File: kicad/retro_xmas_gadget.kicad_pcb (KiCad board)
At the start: 4 copper layers, 76.2 x 101.6 mm, 84 parts, among them J1 USB_C_Receptacle_USB2.0_16P, J2 SD_Card_Receptacle, J3 AudioJack3_SwitchTR, J4 Conn_01x18, J5 Conn_01x02, J6 Conn_01x03, J7 Conn_01x03, J8 Conn_01x07, Q1 UMH3N, Q2 SS8050, SW1 RESET, SW10 SELECT, SW11 START, SW12 A, SW13 B, SW2 BOOT, SW3 KH-SS12F23-G6, SW4 UP, SW5 DOWN, SW6 LEFT, SW7 RIGHT, SW8 MENU, SW9 OPTION, U1 CP2102N-Axx-xQFN28, U2 ESP32-S3-WROOM-1, U4 XC6210B332MR, U5 TP4056

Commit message: improvements and corrections
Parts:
- D1: footprint Diode_SMD:D_SOD-323_HandSoldering -> Diode_SMD:D_SOD-123
- R23: value 5.1k -> 0R
- U3, U5: footprint Package_SO:SOP-8-1EP_4.57x4.57mm_P1.27mm_EP4.57x4.45mm_ThermalVias -> Package_SO:SOIC-8-1EP_3.9x4.9mm_P1.27mm_EP2.41x3.3mm_ThermalVias
- moved C15 9.08 mm to (77.7, 69.3), turned to 0 degrees
- moved C16 4.81 mm to (86.9, 68.5), turned to 0 degrees
- moved J5 3.52 mm to (79.4, 75.3)
- moved C10 3.43 mm to (87.0, 72.3)
- moved C9 3.43 mm to (87.0, 70.5)
- moved U3 1.84 mm to (87.0, 77.5)
- moved R15 1.02 mm to (41.9, 69.3)
- moved R16 1.02 mm to (41.9, 72.9)
- moved L1 0.51 mm to (77.7, 67.2)
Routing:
- net GND: track 100.0 -> 106.6 mm, vias 190 -> 185
- net VCC: track 29.2 -> 33.5 mm
- net /AUDIO+: track 10.8 -> 14.4 mm
- net VBUS: track 81.7 -> 85.1 mm
- net /SPK+: track 11.8 -> 14.4 mm
- net VAA: track 9.72 -> 11.9 mm
- net Net-(U5-PROG): track 2.90 -> 4.57 mm
- net /VBAT: track 34.1 -> 35.6 mm
- net Net-(D3-K): track 89.5 -> 90.6 mm
- net Net-(D4-K): track 85.1 -> 85.9 mm
- net Net-(U5-~{CHRG}): track 2.81 -> 3.47 mm
- net Net-(U5-~{STDBY}): track 2.80 -> 3.46 mm

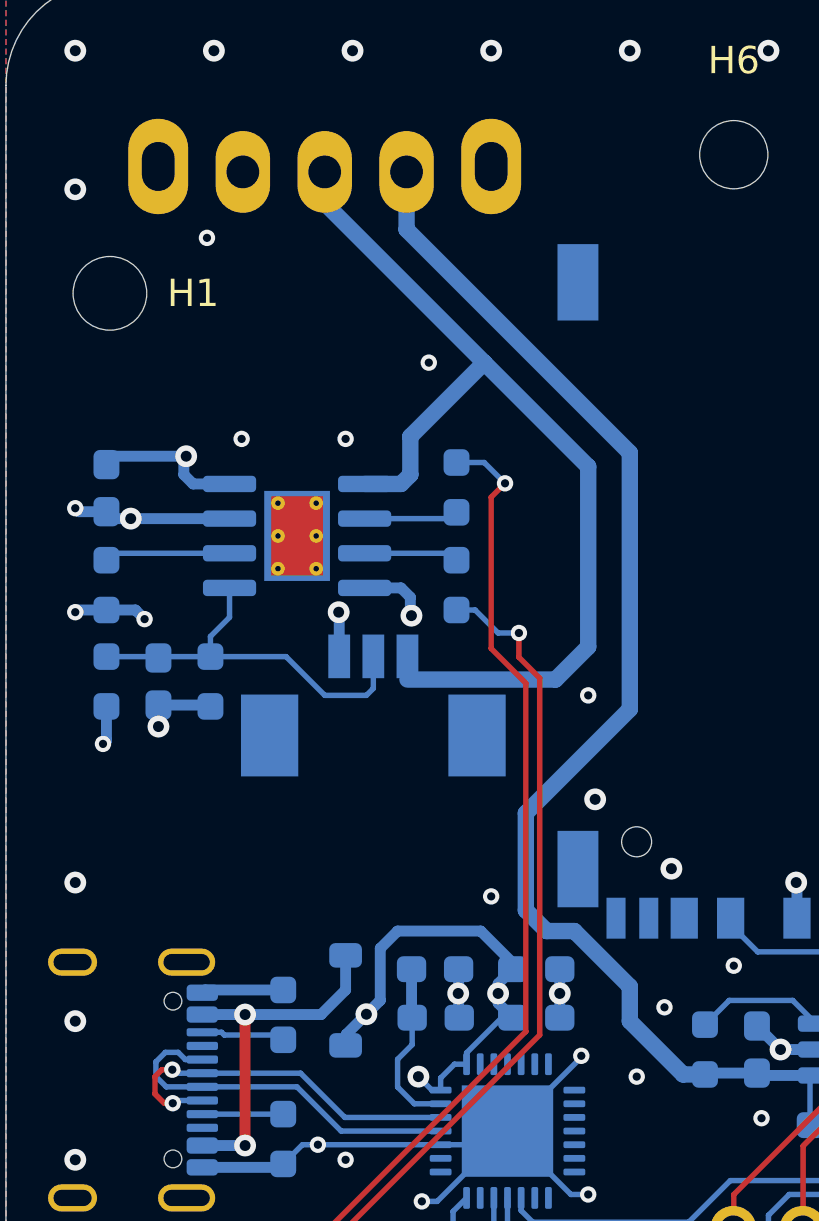
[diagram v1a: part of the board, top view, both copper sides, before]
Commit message: load sharing
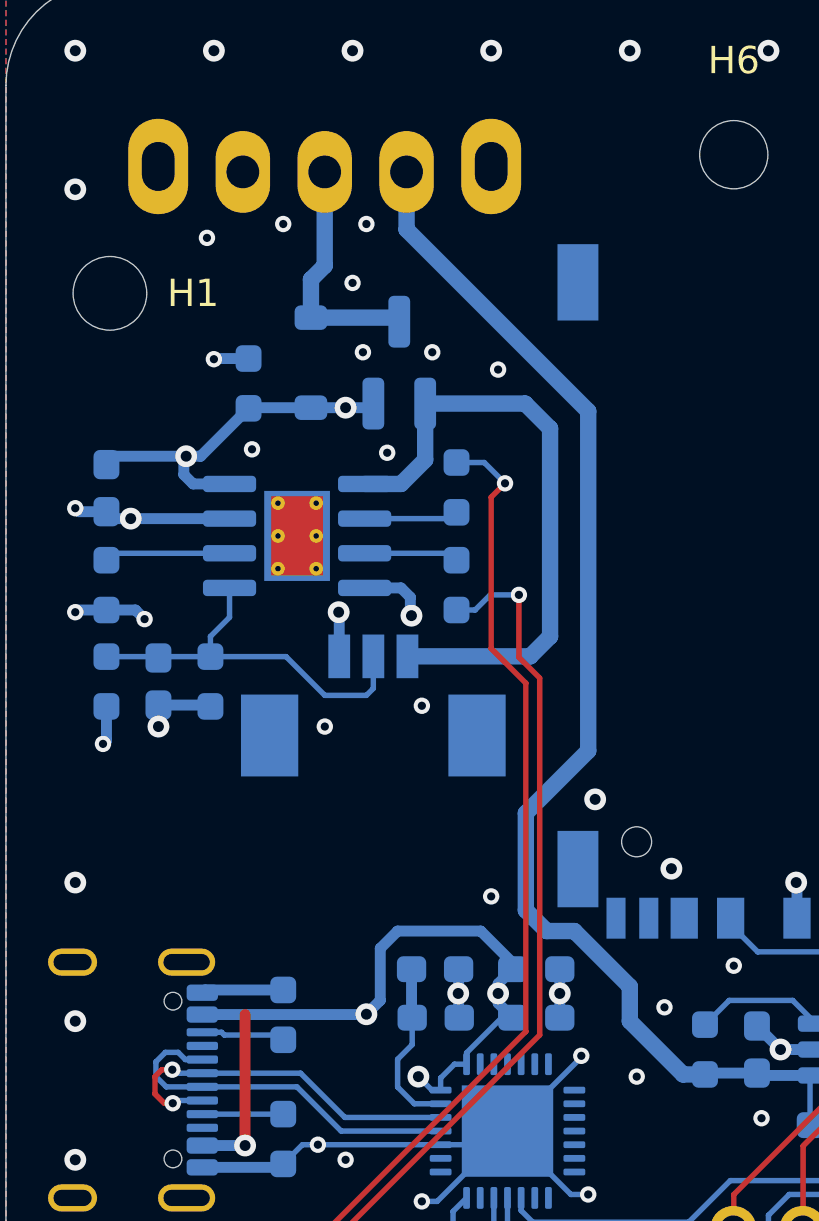
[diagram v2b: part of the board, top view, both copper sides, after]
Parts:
- added Q3: PMOS, Package_TO_SOT_SMD:SOT-23_Handsoldering, B.Cu at (39.8, 64.8)
- added R24: 100K, Resistor_SMD:R_0603_1608Metric_Pad0.98x0.95mm_HandSolder, B.Cu at (34.3, 65.5)
- D1: value BAT54J -> CRS08
- R14: value 2K -> 1.5K
- moved G*** 36.3 mm to (36.4, 100.1)
- moved D1 23.4 mm to (36.6, 64.8), turned to -90 degrees
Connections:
- D1 pad 1: VBUS -> /VBAT_LOAD
- D1 pad 2: Net-(D1-A) -> VBUS
- J1 pad A4: Net-(D1-A) -> VBUS
- J1 pad A9: Net-(D1-A) -> VBUS
- J1 pad B4: Net-(D1-A) -> VBUS
- J1 pad B9: Net-(D1-A) -> VBUS
- SW3 pad 2: /VBAT -> /VBAT_LOAD
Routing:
- net VBUS: track 85.1 -> 103.7 mm, vias 9 -> 11
- net Net-(D1-A): track 13.3 -> 0.00 mm, vias 2 -> 0
- net /VBAT: track 35.6 -> 22.8 mm
- net /VBAT_LOAD: track 0.00 -> 8.85 mm
- net GND: track 106.6 -> 107.8 mm, vias 185 -> 192
- net Net-(D4-K): track 85.9 -> 87.2 mm
- net /VBAT_ON: track 48.4 -> 47.1 mm

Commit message: rearrangement, updates, upgrades
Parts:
- moved G*** 71.7 mm to (96.8, 61.3)
- moved G*** 71.7 mm to (37.6, 99.3)
- moved H1 7.62 mm to (29.2, 54.6)
- moved H2 7.62 mm to (97.8, 54.6)
- moved SW3 2.80 mm to (36.9, 57.8)
- moved J2 2.22 mm to (62.2, 73.2)
- moved U3 2.09 mm to (89.1, 77.5)
- moved J5 1.91 mm to (81.3, 75.3)
- moved J3 1.82 mm to (90.2, 56.7)
- moved C16 1.78 mm to (88.6, 68.5)
- moved R10 1.78 mm to (93.2, 68.0)
- moved R9 1.78 mm to (93.2, 71.5)
- moved C10 1.78 mm to (88.8, 72.3)
- moved C15 1.78 mm to (79.5, 69.3)
- moved C9 1.78 mm to (88.8, 70.5)
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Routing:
- net /SD_DAT: track 35.7 -> 29.8 mm
- net GND: track 107.8 -> 103.5 mm, vias 192 -> 189
- net /VBAT_ON: track 47.1 -> 43.6 mm
- net VCC: track 33.5 -> 36.4 mm
- net VBUS: track 103.7 -> 106.2 mm
- net /TFT_LEDK: track 14.0 -> 16.4 mm
- net /AMP_LRCLK: track 2.83 -> 4.95 mm
- net /SD_CD: track 16.4 -> 14.3 mm
- net /SD_CLK: track 27.1 -> 25.1 mm
- net /SD_CMD: track 20.6 -> 19.0 mm
- net /HJ+: track 27.2 -> 25.8 mm
- net /TFT_LEDA: track 13.6 -> 14.9 mm
- net /RXD: track 59.3 -> 58.0 mm
- net /RTS: track 29.5 -> 28.2 mm
- net Net-(U1-D+): track 13.8 -> 15.0 mm
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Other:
- board text added: "CROKPOCKET XL"
- board text added: "https://github.com/ducalex/retro-go PCB v1.0 by hfvermeer"
- board text removed: "https://github.com/ducalex/retro-go PCB v0.9 by hfvermeer"

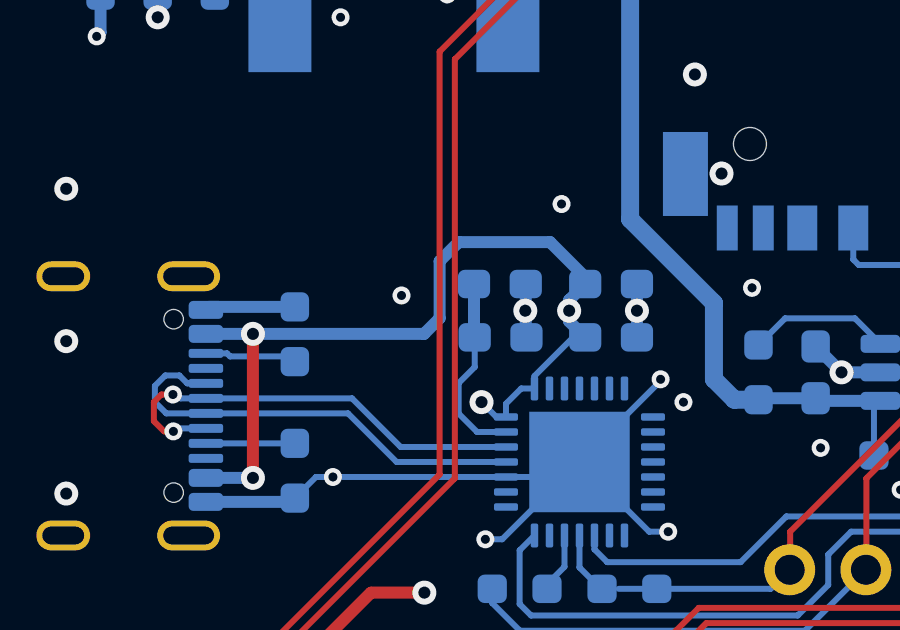
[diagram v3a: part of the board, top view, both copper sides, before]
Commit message: add pull up resistor to cp2102 rst
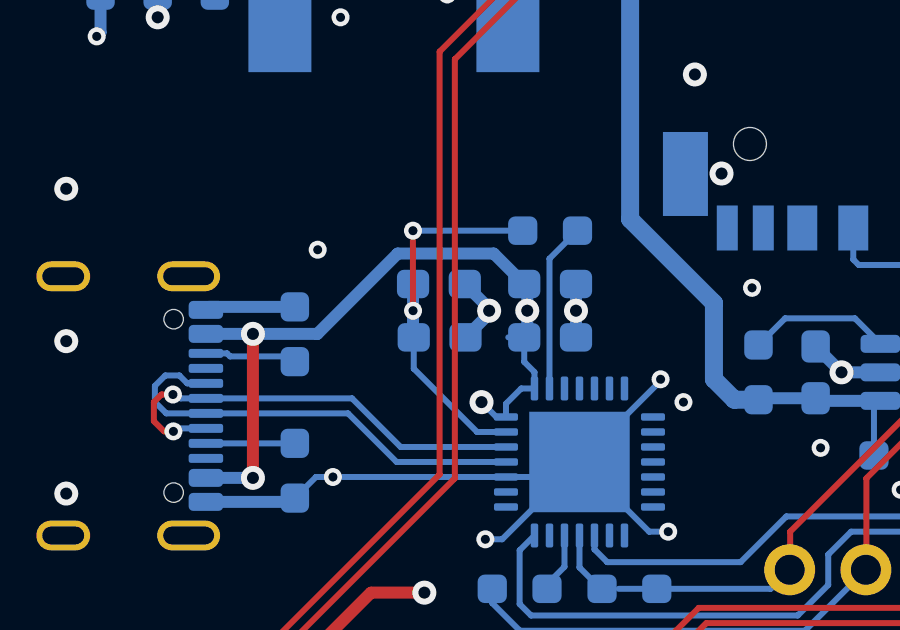
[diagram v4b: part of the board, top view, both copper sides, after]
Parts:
- added R25: 4.7k, Resistor_SMD:R_0603_1608Metric_Pad0.98x0.95mm_HandSolder, B.Cu at (44.1, 85.2)
- moved C4 2.03 mm to (40.4, 87.0)
- moved C1 2.03 mm to (44.1, 88.8)
- moved C2 2.03 mm to (44.1, 87.0)
- moved C3 2.03 mm to (40.4, 88.8)
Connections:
- U1 pad 9: unconnected-(U1-~{RST}-Pad9) -> Net-(U1-~{RST})
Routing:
- net Net-(U1-VDD): track 6.38 -> 13.1 mm, vias 0 -> 2
- net Net-(U1-~{RST}): track 0.00 -> 5.65 mm
- net VBUS: track 106.2 -> 102.2 mm
- net GND: track 103.5 -> 104.2 mm, vias 189 -> 188

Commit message: design check. Gerbers
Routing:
- net /TXD: track 52.3 -> 51.0 mm
- net VBUS: track 102.2 -> 101.7 mm
- net GND: track 104.2 -> 104.3 mm, vias 188 -> 195
- net (no net): vias 1 -> 0
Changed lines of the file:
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@@
 		)
 	)
-	(via
-		(at 50.8 160.02)
-		(size 0.8)
-		(drill 0.4)
-		(layers "F.Cu" "B.Cu")
-		(net 0)
-	)
 	(segment
 		(start 91.42 102.772134)
@@
 	)
 	(via
+		(at 45.466 83.82)
+		(size 0.6)
+		(drill 0.3)
+		(layers "F.Cu" "B.Cu")
+		(free yes)
+		(net 4)
+	)
+	(via
 		(at 27.94 70.104)
 		(size 0.6)
@@
 	)
 	(via
+		(at 45.466 76.454)
+		(size 0.6)
+		(drill 0.3)
+		(layers "F.Cu" "B.Cu")
+		(free yes)
+		(net 4)
+	)
+	(via
 		(at 79.248 106.426)
 		(size 0.6)
@@
 	)
 	(via
+		(at 41.91 84.074)
+		(size 0.6)
+		(drill 0.3)
+		(layers "F.Cu" "B.Cu")
+		(free yes)
+		(net 4)
+	)
+	(via
 		(at 83.058 96.52)
 		(size 0.6)
@@
 	)
 	(via
+		(at 94.742 69.088)
+		(size 0.6)
+		(drill 0.3)
+		(layers "F.Cu" "B.Cu")
+		(free yes)
+		(net 4)
+	)
+	(via
 		(at 42.672 102.616)
 		(size 0.6)
@@
 	)
 	(via
+		(at 44.45 59.69)
+		(size 0.6)
+		(drill 0.3)
+		(layers "F.Cu" "B.Cu")
+		(free yes)
+		(net 4)
+	)
+	(via
 		(at 78.867 113.538)
 		(size 0.6)
@@
 	)
 	(via
+		(at 42.164 81.026)
+		(size 0.6)
+		(drill 0.3)
+		(layers "F.Cu" "B.Cu")
+		(free yes)
+		(net 4)
+	)
+	(via
 		(at 63.5 53.34)
 		(size 0.8)
@@
 	)
 	(via
-		(at 42.037 87.884)
+		(at 42.164 87.884)
 		(size 0.8)
 		(drill 0.4)
@@
 	)
 	(via
+		(at 39.116 83.82)
+		(size 0.6)
+		(drill 0.3)
+		(layers "F.Cu" "B.Cu")
+		(free yes)
+		(net 4)
+	)
+	(via
 		(at 89.6355 73.1785)
 		(size 0.8)
@@
 	)
 	(segment
-		(start 42.037 87.9845)
-		(end 41.2485 88.773)
-		(width 0.4)
-		(layer "B.Cu")
-		(net 4)
-	)
-	(segment
 		(start 41.2485 88.773)
 		(end 41.021 89.0005)
@@
 	)
 	(segment
-		(start 42.037 87.884)
-		(end 42.037 87.807)
+		(start 41.275 88.773)
+		(end 41.2485 88.773)
 		(width 0.4)
 		(layer "B.Cu")
@@
 	)
 	(segment
+		(start 42.164 87.884)
+		(end 41.275 86.995)
+		(width 0.4)
+		(layer "B.Cu")
+		(net 4)
+	)
+	(segment
 		(start 67.2835 99.822)
 		(end 65.1245 97.663)
@@
 	)
 	(segment
+		(start 41.275 86.995)
+		(end 41.225 86.995)
+		(width 0.4)
+		(layer "B.Cu")
+		(net 4)
+	)
+	(segment
 		(start 93.583806 81.67622)
 		(end 93.583273 81.67622)
@@
 	)
 	(segment
-		(start 42.037 87.807)
-		(end 41.225 86.995)
-		(width 0.4)
-		(layer "B.Cu")
-		(net 4)
-	)
-	(segment
 		(start 65.1245 96.4195)
 		(end 65.151 96.393)
@@
 	)
 	(segment
-		(start 36.83 93.427)
-		(end 36.2635 93.427)
-		(width 0.2)
+		(start 42.164 87.884)
+		(end 41.275 88.773)
+		(width 0.4)
 		(layer "B.Cu")
 		(net 4)
 	)
 	(segment
-		(start 42.037 87.884)
-		(end 42.037 87.9845)
-		(width 0.4)
+		(start 36.83 93.427)
+		(end 36.2635 93.427)
+		(width 0.2)
 		(layer "B.Cu")
 		(net 4)
@@
 	)
 	(segment
-		(start 42.674601 88.773)
-		(end 43.2065 88.773)
-		(width 0.2)
-		(layer "B.Cu")
-		(net 8)
-	)
-	(segment
 		(start 34.3145 66.42)
 		(end 34.29 66.4445)
@@
 	)
 	(segment
-		(start 51.42 97.155)
-		(end 52.055 96.52)
+		(start 86.706 89.316)
+		(end 89.916 86.106)
 		(width 0.2)
 		(layer "B.Cu")
@@
 	)
 	(segment
-		(start 86.706 89.316)
-		(end 89.916 86.106)
+		(start 90.15 82.85)
+		(end 90.17 82.85)
 		(width 0.2)
 		(layer "B.Cu")
@@
 	)
 	(segment
-		(start 90.15 82.85)
-		(end 90.17 82.85)
+		(start 47.625 97.155)
+		(end 51.42 97.155)
 		(width 0.2)
 		(layer "B.Cu")
@@
 	)
 	(segment
-		(start 89.916 83.064)
-		(end 90.15 82.83)
+		(start 51.42 97.155)
+		(end 52.055 96.52)
 		(width 0.2)
 		(layer "B.Cu")
@@
 	)
 	(segment
-		(start 46.355 97.155)
-		(end 51.42 97.155)
+		(start 89.916 83.064)
+		(end 90.15 82.83)
 		(width 0.2)
 		(layer "B.Cu")
@@
 	)
 	(segment
-		(start 82.423 89.789)
-		(end 82.423 87.590943)
+		(start 83.058 84.967194)
+		(end 83.058 75.819)
 		(width 0.2)
 		(layer "F.Cu")
@@
 	)
 	(segment
-		(start 77.47 97.282)
-		(end 77.47 94.742)
+		(start 82.423 87.590943)
+		(end 83.312 86.701943)
 		(width 0.2)
 		(layer "F.Cu")
@@
 	)
 	(segment
-		(start 83.058 84.967194)
-		(end 83.058 75.819)
+		(start 78.232 96.52)
+		(end 78.232 93.98)
 		(width 0.2)
 		(layer "F.Cu")
@@
 	)
 	(segment
-		(start 82.423 87.590943)
-		(end 83.312 86.701943)
+		(start 80.6542 73.4152)
+		(end 77.648 73.4152)
 		(width 0.2)
 		(layer "F.Cu")
@@
 	)
 	(segment
-		(start 83.312 86.701943)
-		(end 83.312 85.221194)
+		(start 78.232 93.98)
+		(end 82.423 89.789)
 		(width 0.2)
 		(layer "F.Cu")
@@
 	)
 	(segment
-		(start 80.6542 73.4152)
-		(end 77.648 73.4152)
+		(start 83.058 75.819)
+		(end 80.6542 73.4152)
 		(width 0.2)
 		(layer "F.Cu")
@@
 	)
 	(segment
-		(start 77.47 94.742)
-		(end 82.423 89.789)
+		(start 83.312 86.701943)
+		(end 83.312 85.221194)
 		(width 0.2)
 		(layer "F.Cu")
@@
 	)
 	(segment
-		(start 83.058 75.819)
-		(end 80.6542 73.4152)
+		(start 82.423 89.789)
+		(end 82.423 87.590943)
+		(width 0.2)
+		(layer "F.Cu")
+		(net 73)
+	)
+	(segment
+		(start 77.47 97.282)
+		(end 78.232 96.52)
 		(width 0.2)
 		(layer "F.Cu")

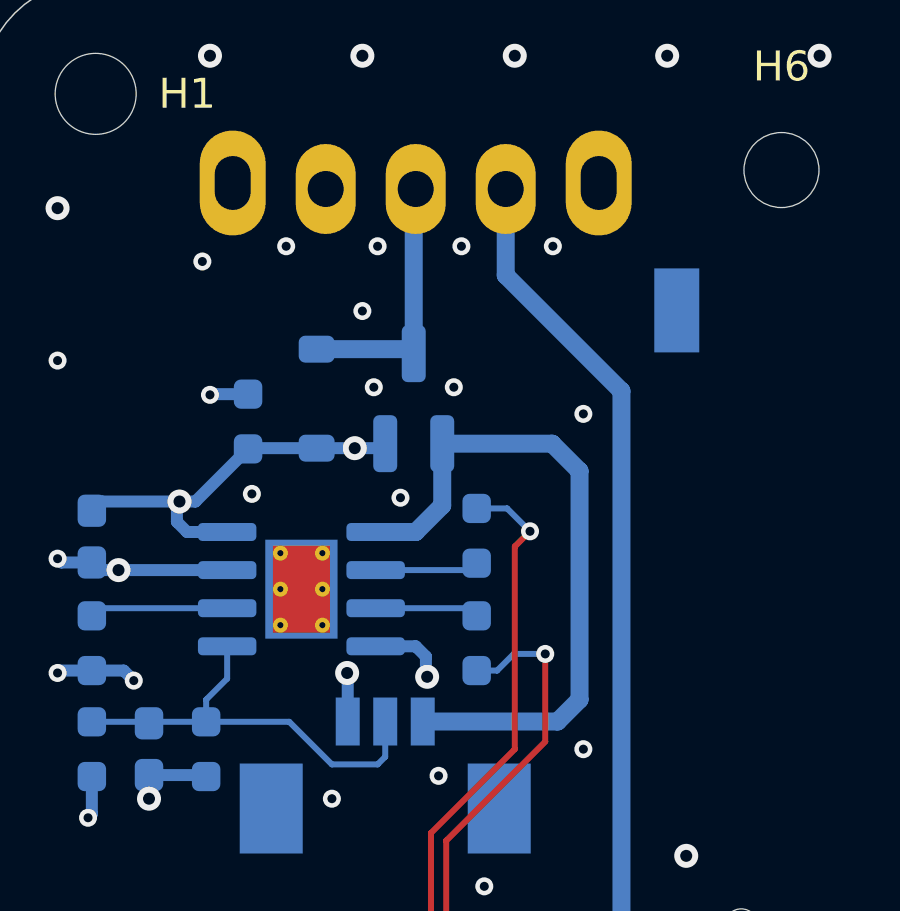
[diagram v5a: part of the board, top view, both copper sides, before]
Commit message: footprint correction
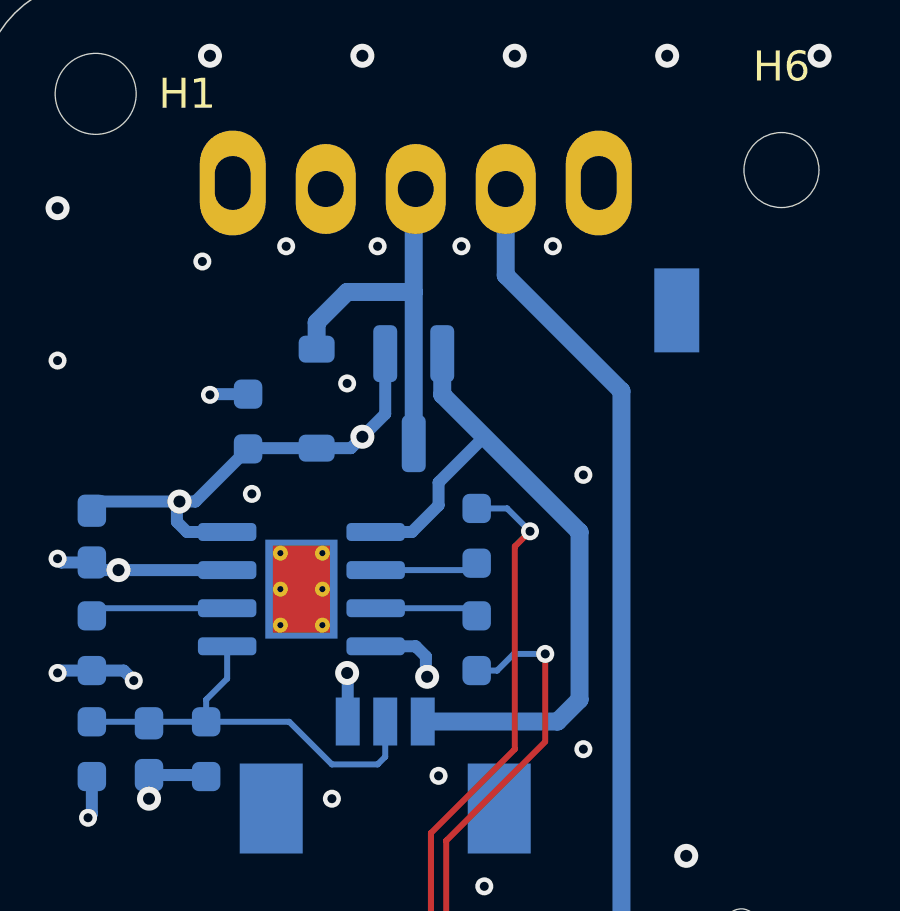
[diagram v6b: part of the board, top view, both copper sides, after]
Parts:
- Q3: value PMOS -> AP3407A
- R17: value 15k -> 5.1K
- R23: value 0R -> 100K
- turned Q3 to -90 degrees
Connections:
- Q3 pad 1: /VBAT -> VBUS
- Q3 pad 2: VBUS -> /VBAT
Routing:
- net /VBAT_LOAD: track 8.81 -> 13.1 mm
- net VBUS: track 101.7 -> 104.1 mm
- net /VBAT: track 22.8 -> 24.3 mm
- net GND: vias 195 -> 192
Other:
- board text added: "${REFERENCE}"
- board text added: "https://github.com/ducalex/retro-go PCB v1.1 by hfvermeer"
- board text removed: "https://github.com/ducalex/retro-go PCB v1.0 by hfvermeer"

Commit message: component change
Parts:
- Q3: value AP3407A -> SI2301CDS
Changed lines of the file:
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@@
 			)
 		)
-		(property "Value" "AP3407A"
+		(property "Value" "SI2301CDS"
 			(at 0 -2.5 90)
 			(layer "B.Fab")
